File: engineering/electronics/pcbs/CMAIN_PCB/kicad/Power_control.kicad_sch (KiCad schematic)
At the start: 34 parts, among them K1 CPC1019N, K2 CPC1019N, K3 CPC1019N, Q1 SIRA99DP-T1-GE3, Q2 SIRA99DP-T1-GE3, Q3 SIR570DP-T1-RE3

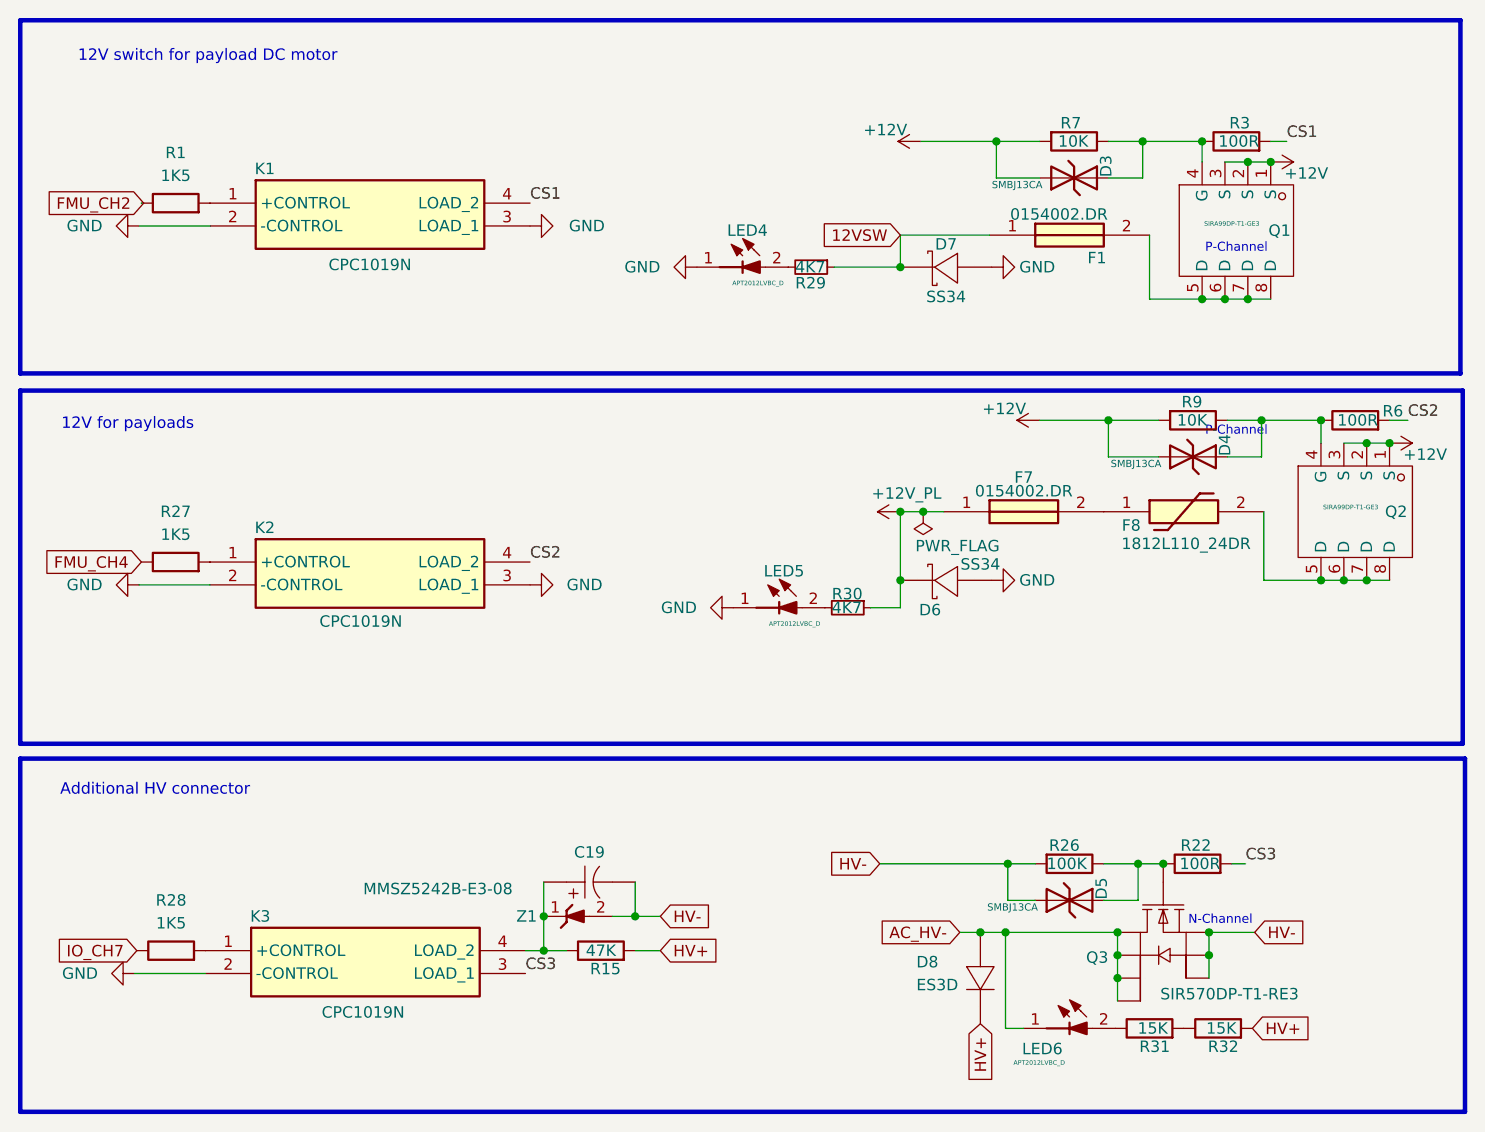
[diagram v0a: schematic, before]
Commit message: Import linked CMAIN PCB layout
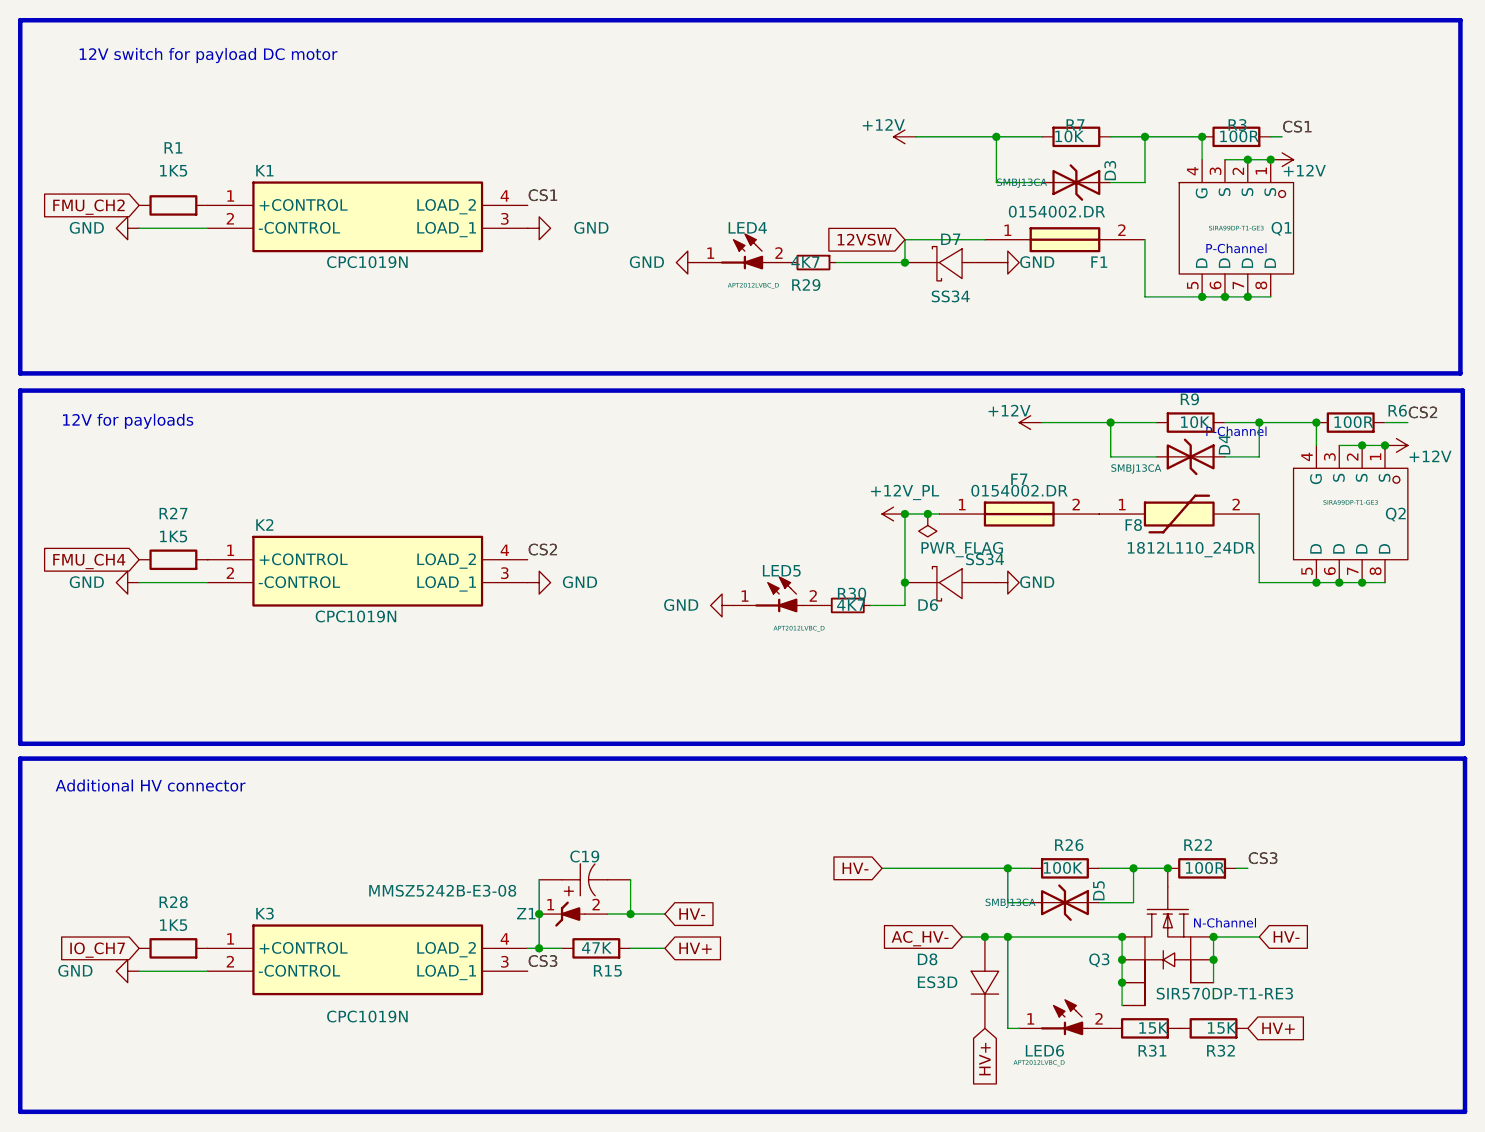
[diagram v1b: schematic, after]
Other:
- moved on the sheet: C19, D3, D5, D6, D7, D8, F1, F7, F8, LED4, LED6, Q2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

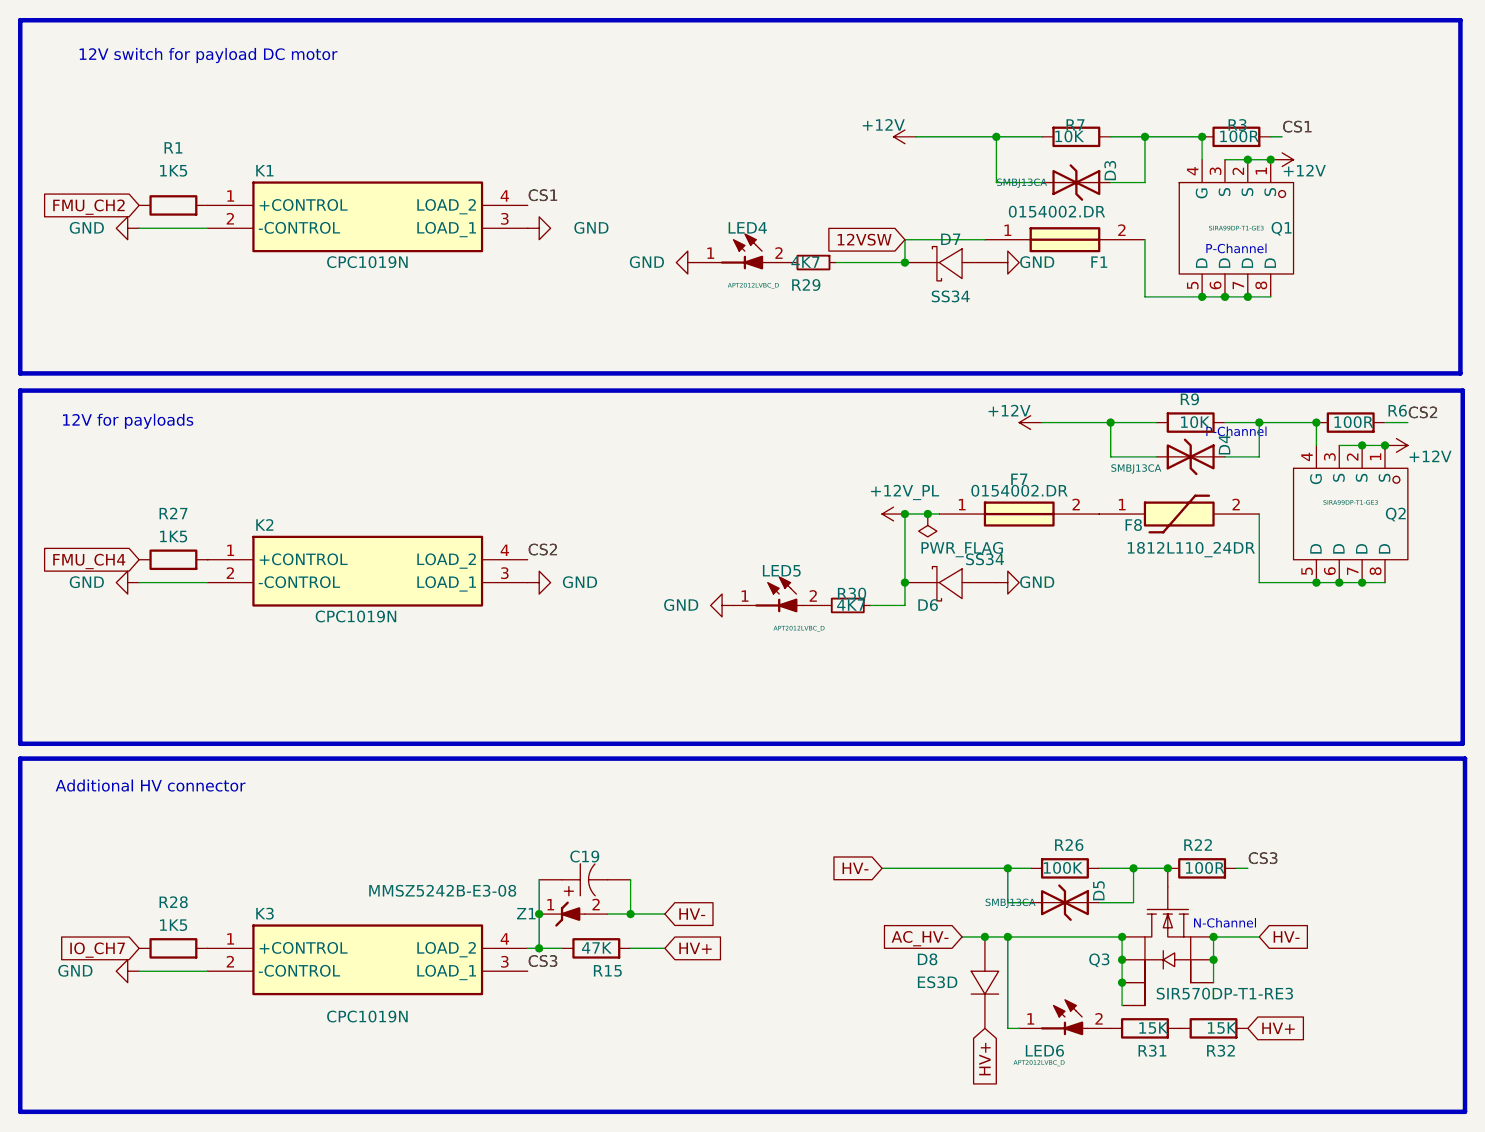
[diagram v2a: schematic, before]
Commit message: electronics: integrate June PCB updates
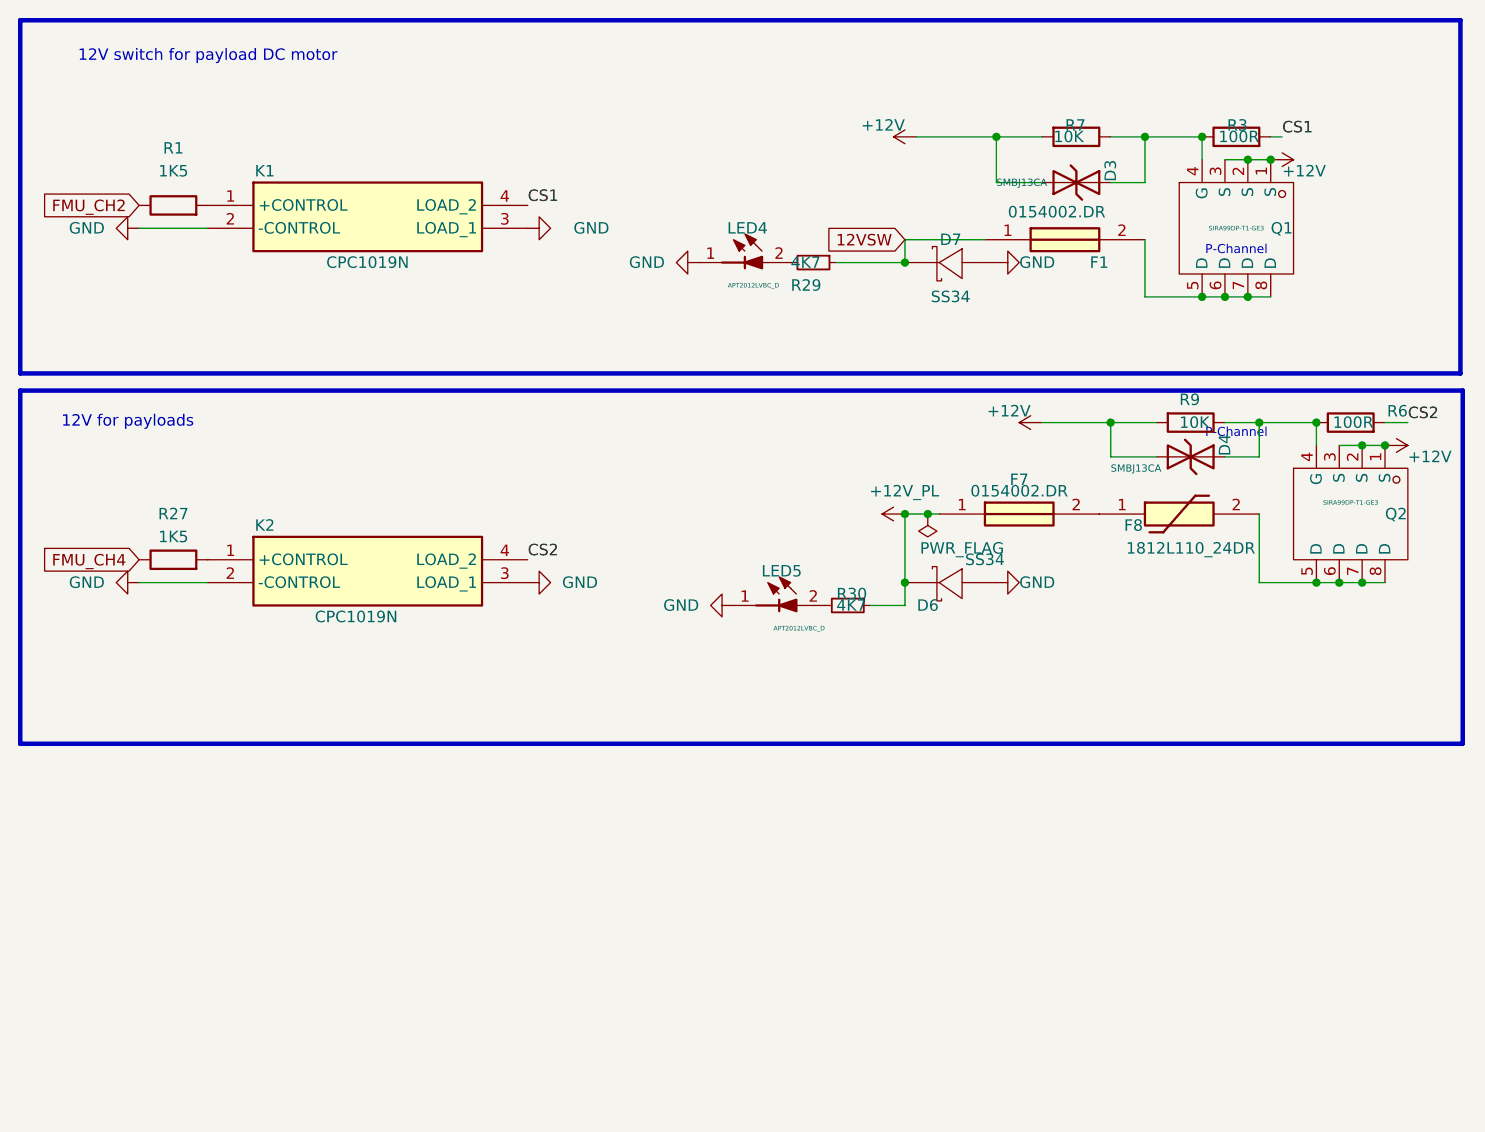
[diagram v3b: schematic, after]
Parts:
- removed C19: 22uF, EasyEDA_Lib:CAP-SMD_L7.3-W4.3-RD_PA300LV227M0J, symbol EasyEDA_Lib:EEFCX1E220R
- removed D5: SMBJ13CA, PCM_JLCPCB:D_SMB, symbol PCM_JLCPCB-Diodes:TVS-Bi,SMBJ13CA
- removed D8: ES3D, EasyEDA_Lib:SMC_L7.1-W6.2-LS8.1-RD, symbol Snapeda:ES3D_C241735
- removed K3: CPC1019N, Samacsys:SOP254P610X218-4N, symbol Samacsys_kicad_sym:CPC1019N
- removed LED6: APT2012LVBC_D, Samacsys_kicad_sym:LEDC2012X85N, symbol Samacsys_kicad_sym:APT2012LVBC_D
- removed Q3: SIR570DP-T1-RE3, EasyEDA_Lib:POWERPAK-SO-8_L5.9-W4.9-P1.27-LS6.2-BL, symbol Snapeda:SIR570DP-T1-RE3
- removed R15: 47K, Resistor_SMD:R_0805_2012Metric_Pad1.20x1.40mm_HandSolder, symbol Device:R
- removed R22: 100R, Resistor_SMD:R_0805_2012Metric_Pad1.20x1.40mm_HandSolder, symbol Device:R
- removed R26: 100K, Resistor_SMD:R_0805_2012Metric_Pad1.20x1.40mm_HandSolder, symbol Device:R
- removed R28: 1K5, Resistor_SMD:R_0805_2012Metric_Pad1.20x1.40mm_HandSolder, symbol Device:R
- removed R31, R32: 15K, Resistor_SMD:R_0805_2012Metric_Pad1.20x1.40mm_HandSolder, symbol Device:R
- removed Z1: MMSZ5242B-E3-08, Samacsys:SOD3716X135N, symbol Samacsys:MMSZ5242B-E3-08
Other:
- note removed: "Additional HV connector"
- note removed: "N-Channel"

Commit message: electronics: clean up CMAIN local libraries
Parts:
- D3, D4: footprint PCM_JLCPCB:D_SMB -> CMAIN_PCB:D_SMB
- D6, D7: footprint EasyEDA_Lib:SMB_L4.6-W3.6-LS5.3-RD -> CMAIN_PCB:SMB_L4.6-W3.6-LS5.3-RD
- F1, F7: footprint Samacsys:0154002DR -> CMAIN_PCB:0154002DR
- F8: footprint Samacsys:1812L010DR -> CMAIN_PCB:1812L010DR
- K1, K2: footprint Samacsys:SOP254P610X218-4N -> CMAIN_PCB:SOP254P610X218-4N
- LED4, LED5: footprint Samacsys_kicad_sym:LEDC2012X85N -> CMAIN_PCB:LEDC2012X85N
- Q1, Q2: footprint EasyEDA_Lib:POWERPAK-SO-8_L5.9-W4.9-P1.27-LS6.2-BL -> CMAIN_PCB:POWERPAK-SO-8_L5.9-W4.9-P1.27-LS6.2-BL
- R1, R27, R29, R3, R30, R6, R7, R9: footprint Resistor_SMD:R_0805_2012Metric_Pad1.20x1.40mm_HandSolder -> CMAIN_PCB:R_0805_2012Metric_Pad1.20x1.40mm_HandSolder

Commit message: electronics: update CMAIN PCB from June layout
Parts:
- Q1, Q2: footprint CMAIN_PCB:POWERPAK-SO-8_L5.9-W4.9-P1.27-LS6.2-BL -> EasyEDA_Lib:POWERPAK-SO-8_L5.9-W4.9-P1.27-LS6.2-BL
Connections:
- net at D4.2, R6.1, R9.1: now also Q2.2 (G); no longer Q2.4 (G)
- net at D3.2, R3.1, R7.1: now also Q1.2 (G); no longer Q1.4 (G)
- net +12V renamed 12V_3
- net 12V_3: no longer Q1.2 (S), Q1.3 (S), Q2.2 (S), Q2.3 (S)
- new net: F1.2, Q1.3 (D)
- new net: F8.2, Q2.3 (D)
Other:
- moved on the sheet: D4, D6, F7, F8, LED5, Q2, R30, R6, R9

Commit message: electronics: shorten CMAIN footprint filenames for Windows
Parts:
- Q1, Q2: footprint EasyEDA_Lib:POWERPAK-SO-8_L5.9-W4.9-P1.27-LS6.2-BL -> EasyEDA_Lib:fp_a2a0cc2e74
- R1, R27, R29, R3, R30, R6, R7, R9: footprint CMAIN_PCB:R_0805_2012Metric_Pad1.20x1.40mm_HandSolder -> CMAIN_PCB:fp_9fb50b8536
